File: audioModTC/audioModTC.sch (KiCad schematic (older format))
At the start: 40 parts

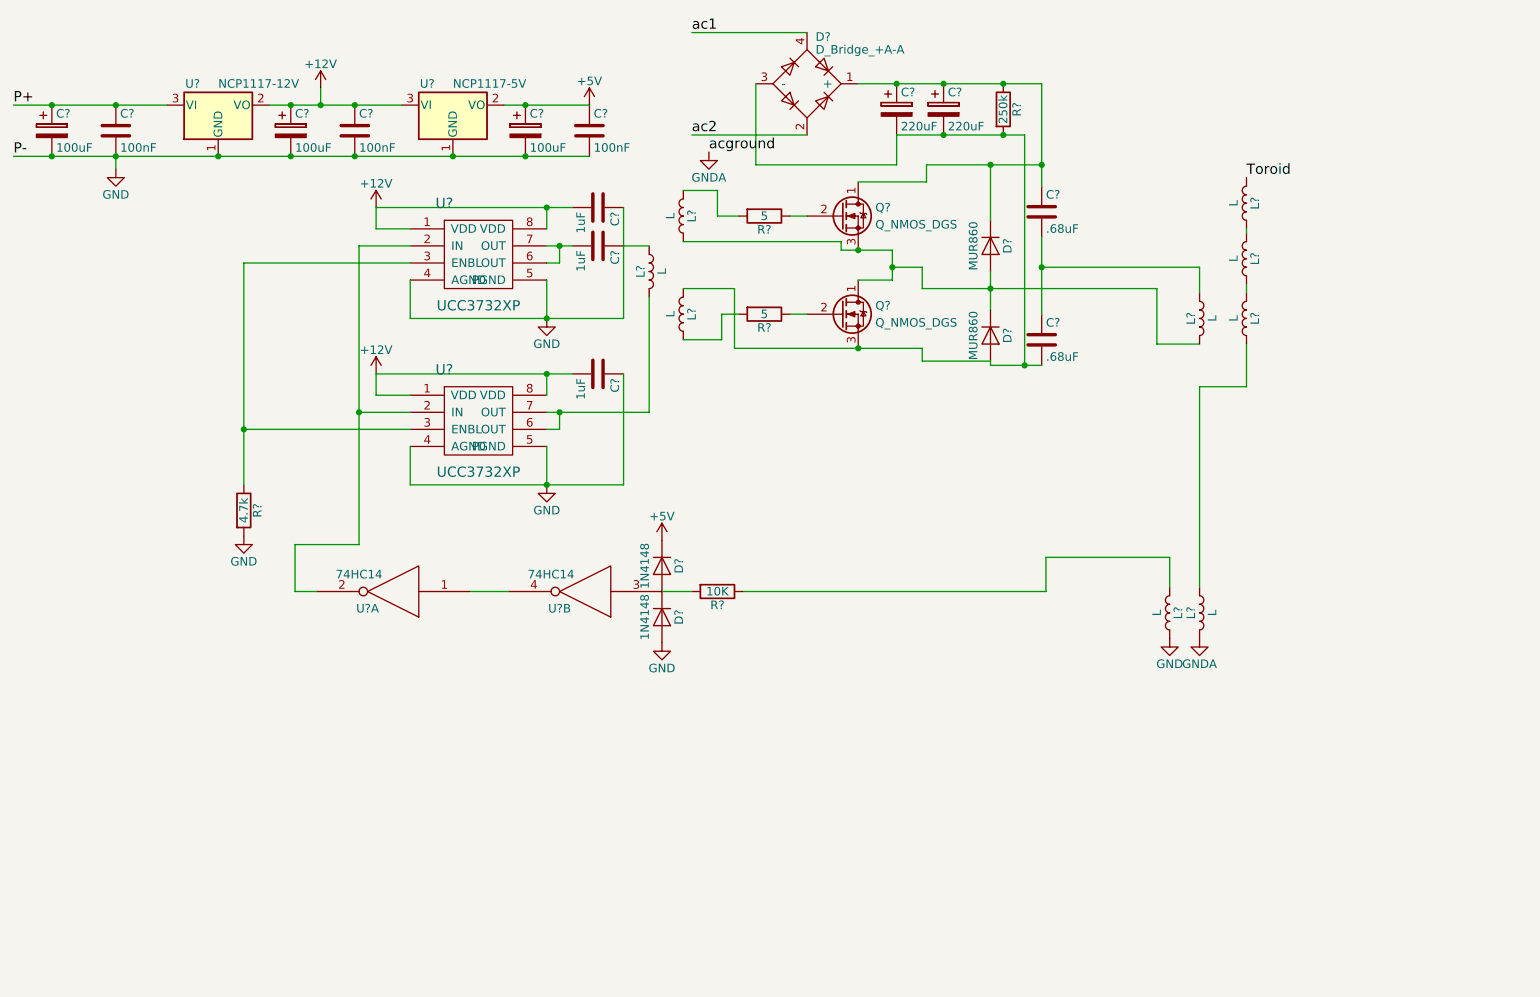
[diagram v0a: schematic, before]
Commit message: Finished Schematic, about to annotate
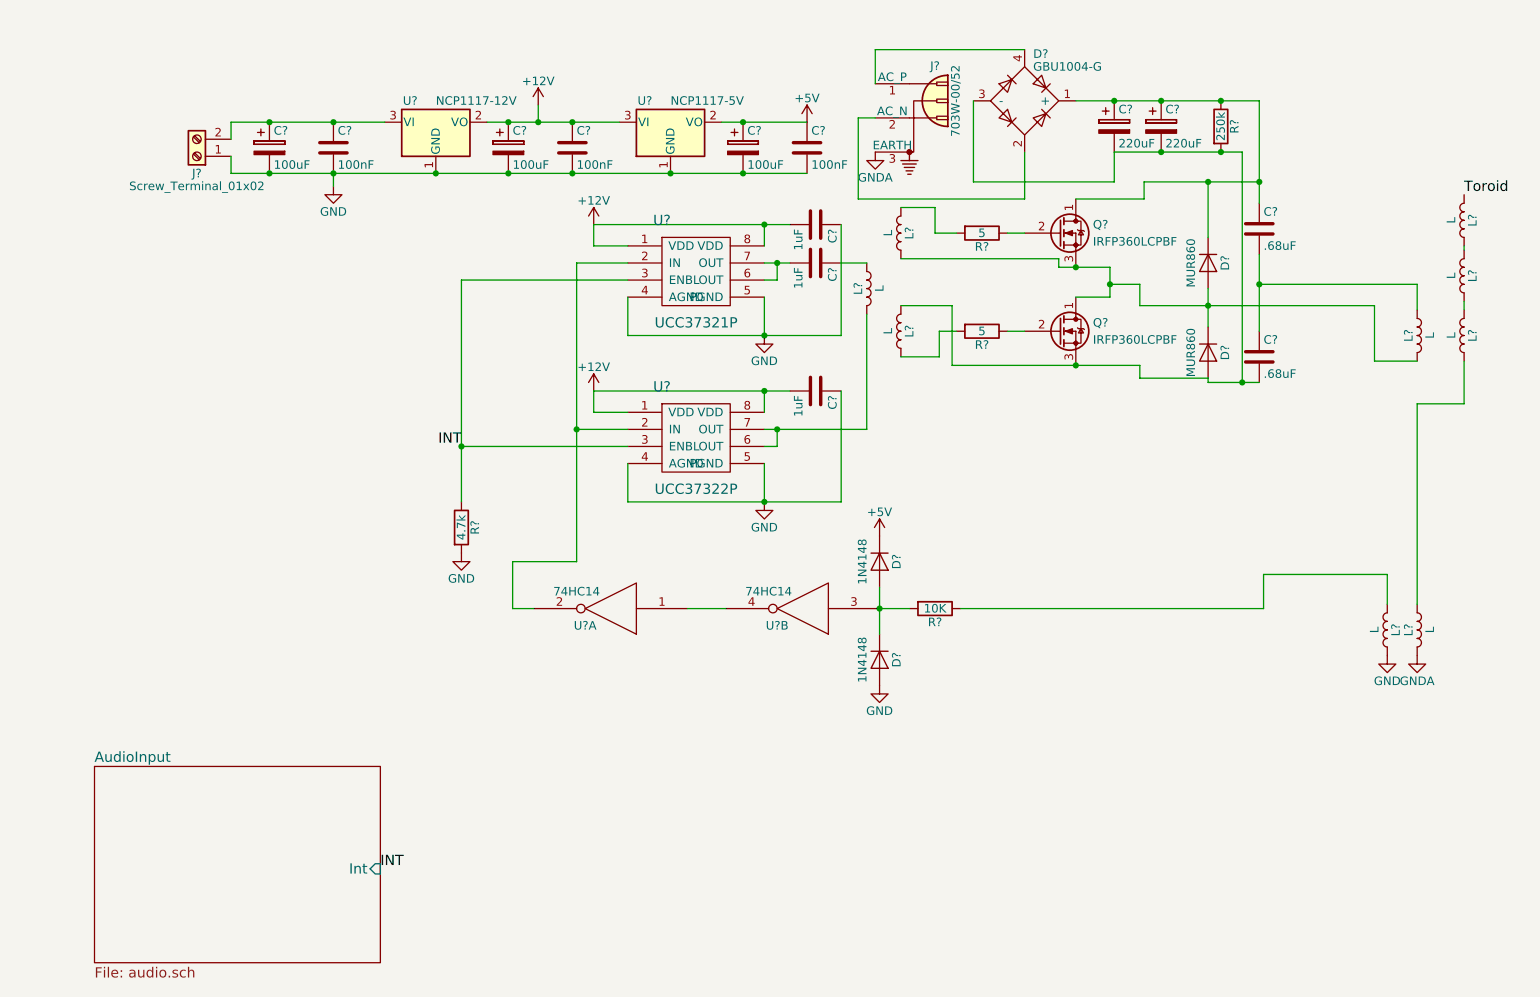
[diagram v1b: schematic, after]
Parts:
- added J?: Screw_Terminal_01x02, symbol Screw_Terminal_01x02
- added J?: 703W-00/52, symbol Conn_WallSocket_Earth
- D?: value D_Bridge_+A-A -> GBU1004-G
- Q? (x2): value Q_NMOS_DGS -> IRFP360LCPBF
- U?: value UCC3732XP -> UCC37321P
- U?: value UCC3732XP -> UCC37322P
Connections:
- net GND: now also J?.1 (Pin_1)
- net GNDA: now also J?.3 (EARTH)
- net INT: now reaches R?.1, U?.3 (ENBL), U?.3 (ENBL)
- net P+: no longer names the net of C?.1, C?.1, U?.3 (VI)
- net P+: now also J?.2 (Pin_2)
- net ac1: no longer names the net of D?.4
- net ac1: now also J?.1 (AC_P)
- net ac2: no longer names the net of D?.2
- net ac2: now also J?.2 (AC_N)
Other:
- moved on the sheet: C?, D?, L?, Q?, R?, U?, U?A, U?B

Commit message: Made some footprints
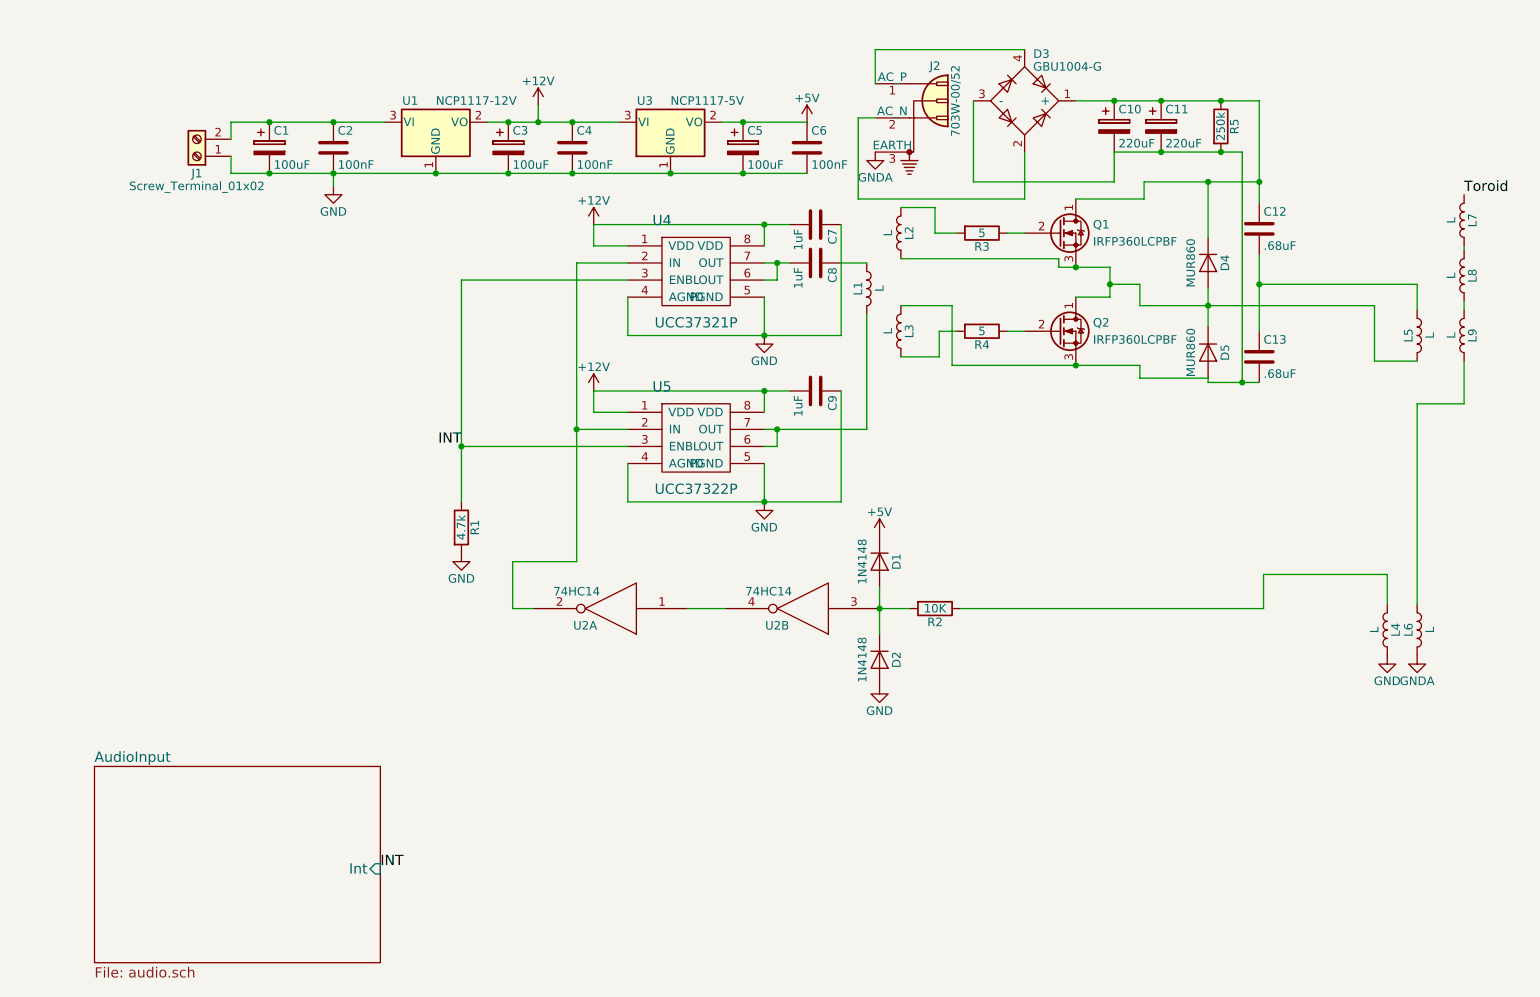
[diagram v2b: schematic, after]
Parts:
- C1, C3, C5: renamed from C?; footprint (none) -> Capacitors_THT:CP_Radial_D12.5mm_P5.00mm
- C10, C11: renamed from C?; footprint (none) -> Capacitors_THT:CP_Radial_D6.3mm_P2.50mm
- C12, C13, C2, C4, C6, C7, C8, C9: renamed from C?; footprint (none) -> Capacitors_SMD:C_0603
- D1, D2: renamed from D?; footprint (none) -> Diodes_SMD:D_SOD-323
- gave numbers to parts that had none: 26

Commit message: Assigned more footprints
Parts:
- D3: footprint (none) -> Custom:4-SIP-5mmPitch
- D4, D5: footprint (none) -> TO_SOT_Packages_THT:TO-220-2_Vertical
- J1: footprint (none) -> TerminalBlocks_Phoenix:TerminalBlock_Phoenix_PT-3.5mm_2pol
- J2: footprint (none) -> Custom:703W-00
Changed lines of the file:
@@
 F 0 "D3" H 6950 1475 50  0000 L CNN
 F 1 "GBU1004-G" H 6950 1400 50  0000 L CNN
-F 2 "" H 6900 1200 50  0001 C CNN
+F 2 "Custom:4-SIP-5mmPitch" H 6900 1200 50  0001 C CNN
 F 3 "" H 6900 1200 50  0001 C CNN
 	1    6900 1200
@@
 F 0 "D4" H 7975 2250 50  0000 C CNN
 F 1 "MUR860" H 7975 2050 50  0000 C CNN
-F 2 "" H 7975 2150 50  0001 C CNN
+F 2 "TO_SOT_Packages_THT:TO-220-2_Vertical" H 7975 2150 50  0001 C CNN
 F 3 "" H 7975 2150 50  0001 C CNN
 	1    7975 2150
@@
 F 0 "D5" H 7975 2775 50  0000 C CNN
 F 1 "MUR860" H 7975 2575 50  0000 C CNN
-F 2 "" H 7975 2675 50  0001 C CNN
+F 2 "TO_SOT_Packages_THT:TO-220-2_Vertical" H 7975 2675 50  0001 C CNN
 F 3 "" H 7975 2675 50  0001 C CNN
 	1    7975 2675
@@
 F 0 "J1" H 2050 1625 50  0000 C CNN
 F 1 "Screw_Terminal_01x02" H 2050 1700 50  0000 C CNN
-F 2 "" H 2050 1525 50  0001 C CNN
+F 2 "TerminalBlocks_Phoenix:TerminalBlock_Phoenix_PT-3.5mm_2pol" H 2050 1525 50  0001 C CNN
 F 3 "" H 2050 1525 50  0001 C CNN
 	1    2050 1525
@@
 F 0 "J2" H 6375 1575 50  0000 C BNN
 F 1 "703W-00/52" V 6525 1400 50  0000 C BNN
-F 2 "" H 5925 1400 50  0001 C CNN
+F 2 "Custom:703W-00" H 5925 1400 50  0001 C CNN
 F 3 "" H 5925 1400 50  0001 C CNN
 	1    6225 1300

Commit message: Made more footprints
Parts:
- Q1, Q2: footprint (none) -> TO_SOT_Packages_THT:TO-247_TO-3P_Vertical
- R1, R2, R3, R4, R5: footprint (none) -> Resistors_SMD:R_0603
- U1, U3: footprint TO_SOT_Packages_SMD:SOT-223-3Lead_TabPin2 -> TO_SOT_Packages_SMD:TO-252-2
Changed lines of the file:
@@
 F 0 "U1" H 3300 1450 50  0000 C CNN
 F 1 "NCP1117-12V" H 3450 1450 50  0000 L CNN
-F 2 "TO_SOT_Packages_SMD:SOT-223-3Lead_TabPin2" H 3450 1525 50  0001 C CNN
+F 2 "TO_SOT_Packages_SMD:TO-252-2" H 3450 1525 50  0001 C CNN
 F 3 "" H 3550 1075 50  0001 C CNN
 	1    3450 1325
@@
 F 0 "U3" H 4675 1450 50  0000 C CNN
 F 1 "NCP1117-5V" H 4825 1450 50  0000 L CNN
-F 2 "TO_SOT_Packages_SMD:SOT-223-3Lead_TabPin2" H 4825 1525 50  0001 C CNN
+F 2 "TO_SOT_Packages_SMD:TO-252-2" H 4825 1525 50  0001 C CNN
 F 3 "" H 4925 1075 50  0001 C CNN
 	1    4825 1325
@@
 F 0 "R5" V 8130 1350 50  0000 C CNN
 F 1 "250k" V 8050 1350 50  0000 C CNN
-F 2 "" V 7980 1350 50  0001 C CNN
+F 2 "Resistors_SMD:R_0603" V 7980 1350 50  0001 C CNN
 F 3 "" H 8050 1350 50  0001 C CNN
 	1    8050 1350
@@
 F 0 "Q2" H 7300 2600 50  0000 L CNN
 F 1 "IRFP360LCPBF" H 7300 2500 50  0000 L CNN
-F 2 "" H 7300 2650 50  0001 C CNN
+F 2 "TO_SOT_Packages_THT:TO-247_TO-3P_Vertical" H 7300 2650 50  0001 C CNN
 F 3 "" H 7100 2550 50  0001 C CNN
 	1    7100 2550
@@
 F 0 "Q1" H 7300 2025 50  0000 L CNN
 F 1 "IRFP360LCPBF" H 7300 1925 50  0000 L CNN
-F 2 "" H 7300 2075 50  0001 C CNN
+F 2 "TO_SOT_Packages_THT:TO-247_TO-3P_Vertical" H 7300 2075 50  0001 C CNN
 F 3 "" H 7100 1975 50  0001 C CNN
 	1    7100 1975
@@
 F 0 "R3" V 6730 1975 50  0000 C CNN
 F 1 "5" V 6650 1975 50  0000 C CNN
-F 2 "" V 6580 1975 50  0001 C CNN
+F 2 "Resistors_SMD:R_0603" V 6580 1975 50  0001 C CNN
 F 3 "" H 6650 1975 50  0001 C CNN
 	1    6650 1975
@@
 F 0 "R4" V 6730 2550 50  0000 C CNN
 F 1 "5" V 6650 2550 50  0000 C CNN
-F 2 "" V 6580 2550 50  0001 C CNN
+F 2 "Resistors_SMD:R_0603" V 6580 2550 50  0001 C CNN
 F 3 "" H 6650 2550 50  0001 C CNN
 	1    6650 2550
@@
 F 0 "R1" V 3680 3700 50  0000 C CNN
 F 1 "4.7k" V 3600 3700 50  0000 C CNN
-F 2 "" V 3530 3700 50  0001 C CNN
+F 2 "Resistors_SMD:R_0603" V 3530 3700 50  0001 C CNN
 F 3 "" H 3600 3700 50  0001 C CNN
 	1    3600 3700
@@
 F 0 "R2" V 6455 4175 50  0000 C CNN
 F 1 "10K" V 6375 4175 50  0000 C CNN
-F 2 "" V 6305 4175 50  0001 C CNN
+F 2 "Resistors_SMD:R_0603" V 6305 4175 50  0001 C CNN
 F 3 "" H 6375 4175 50  0001 C CNN
 	1    6375 4175
